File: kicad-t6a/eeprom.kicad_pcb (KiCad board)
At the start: 2 copper layers, 41 x 20.3 mm, 15 parts, among them J1 PMOD_02x06, J2 PMOD_02x06, SW1 SW_DIP_x04, U1 M24M01-R

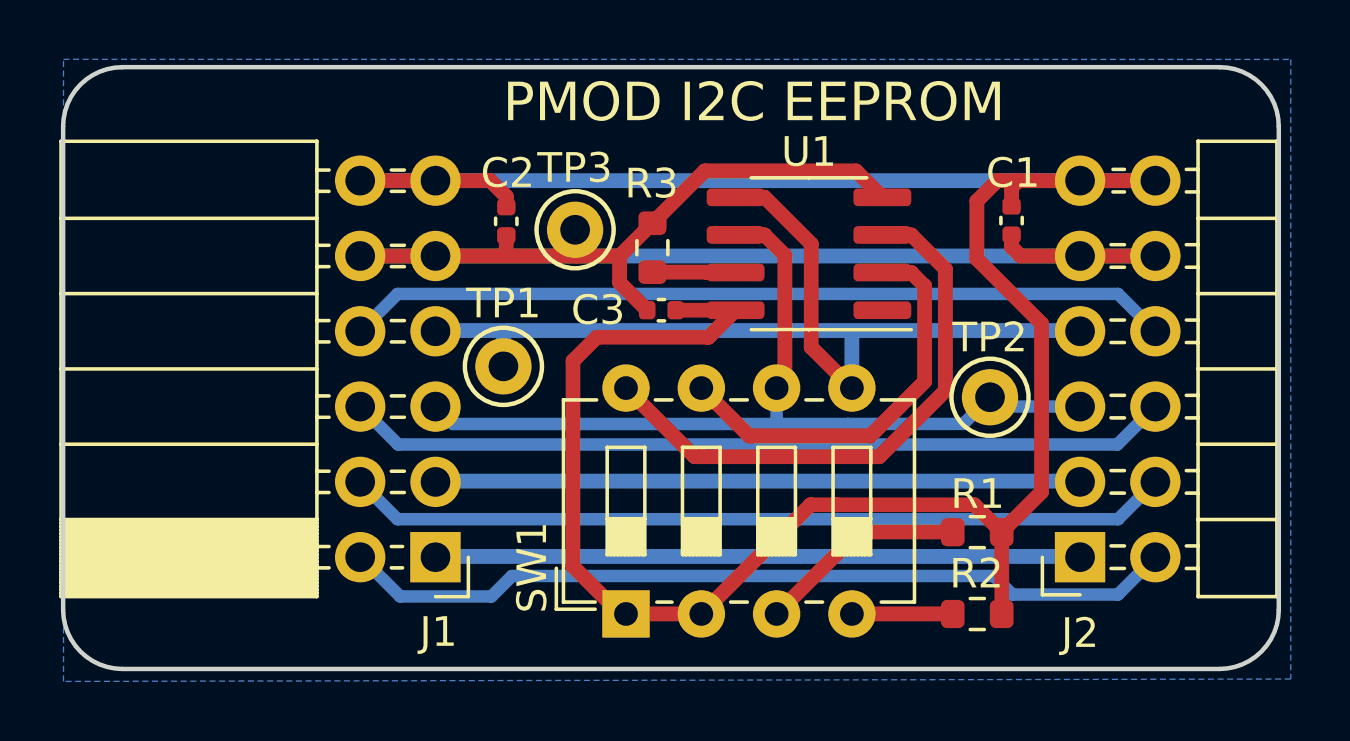
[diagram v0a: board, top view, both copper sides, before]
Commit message: KiCad v7 upgrade, manual workflow trigger
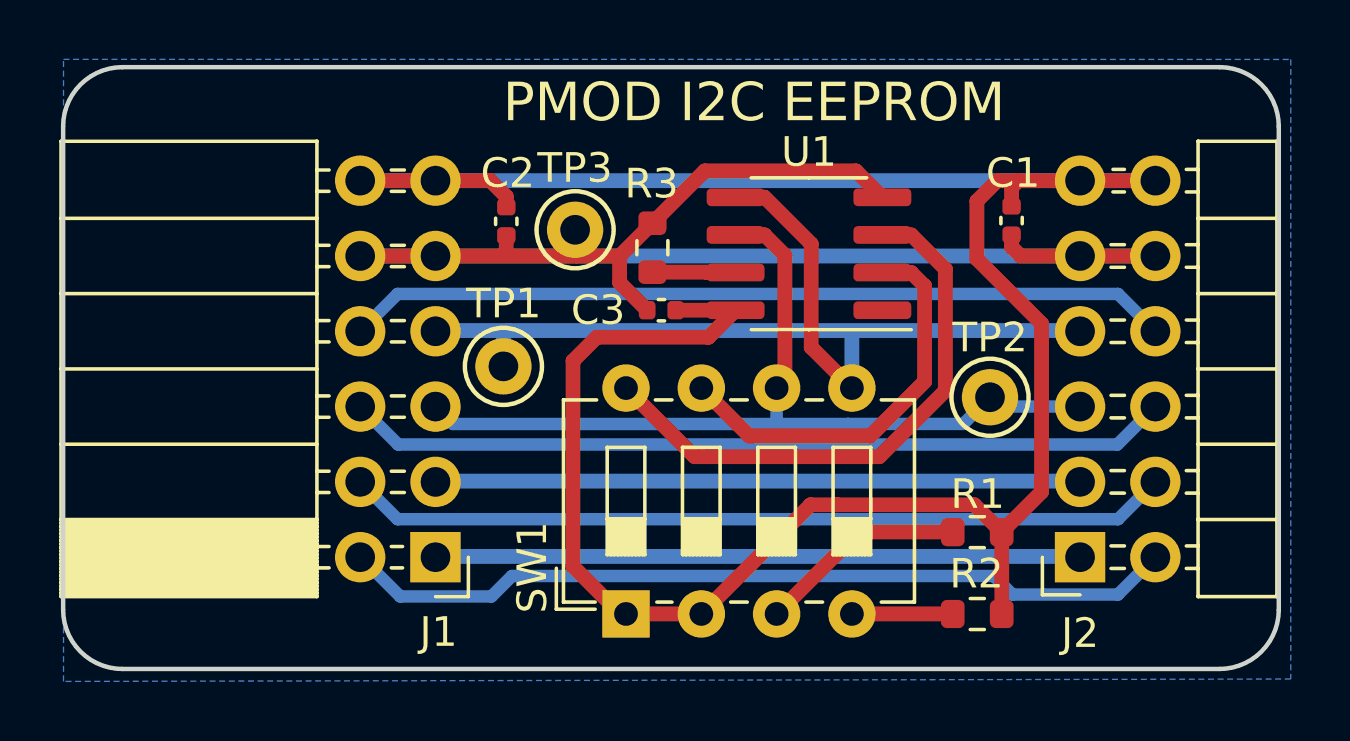
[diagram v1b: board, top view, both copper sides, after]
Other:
- net class 0.25 SMD removed
- net class Default removed
